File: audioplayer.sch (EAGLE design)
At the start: 16 parts, among them J1 MICRO-SDCARD-CONNECTOR-330006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, J2 JST-2P-SMD-PW-3410050P1, J3 MICRO-USB-5P-340015001, J4 CONNECTOR-HEADER-2X3P-3460180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, J5 AUDIO-CONNECTOR-6P-SMD-344003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, K1 BUTTON-4P-3100010P1, U1 ATMEGA328P-AU-1030060P1, U2 CN3065-1320040P1, U3 XC6206-3.3-1300260P1, U4 LM386M-1100070P1, X1 CRYSTAL-0500290P1

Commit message: 1 hr: Finished basic components and schematic.
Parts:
- removed U4: LM386M-1100070P1, OPL:LM386M-1100070P1
- added C10: 100nF, OPL:C-0603
- added C5: 22uF, OPL:C-POLAR-B
- added C6, C7: 10uF, OPL:C-POLAR-A
- added C8, C9: 1uF, OPL:C-0805
- added J6: SCREW-TERMINAL-2P-3470070P1, OPL:SCREW-TERMINAL-2P-3470070P1
- added J7: CONNECTOR-HEADER-6P-3460650P1, OPL:CONNECTOR-HEADER-6P-3460650P1
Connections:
- new net DTR: C10.1, J7.6
- new net N$1: C6.2, C7.1
- new net N$3: J7.2
- new net RX: J7.4, U1.PD0(RXD)
- new net TX: J7.5, U1.PD1(TXD)
- new net VBAT: C6.1, C8.2, J2.+, U2.BAT, U2.FB, U3.VIN
- net 3V3: now also C9.2, J7.3, U3.VOUT
- net 5V: now also C5.1, U2.VIN
- net AUDIO: now also J6.2
- net GND: now also C5.2, C7.2, C8.1, C9.1, J2.-, J6.1, J7.1, U2.GND, U2.TEMP, U3.VSS
- net RESET: now also C10.2
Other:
- moved on the sheet: J2, J3, U2, U3

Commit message: 0.25 hrs: initial placement of components on board.
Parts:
- added R1: (no value), OPL:R-0603
- renumbered R30 to R2
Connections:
- new net N$2: R1.2, U2.ISET
- net GND: now also R1.1
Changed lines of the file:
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@@
 <part name="J2" library="OPL" deviceset="JST-2P-SMD-PW" device="-3410050P1"/>
 <part name="U2" library="OPL" deviceset="CN3065" device="-1320040P1"/>
-<part name="R30" library="OPL" deviceset="R*" device="-0603" value="10K"/>
+<part name="R2" library="OPL" deviceset="R*" device="-0603" value="10K"/>
 <part name="U3" library="OPL" deviceset="XC6206-3.3" device="-1300260P1"/>
 <part name="J3" library="OPL" deviceset="MICRO-USB-5P" device="-340015001"/>
@@
 <part name="J7" library="OPL" deviceset="CONNECTOR-HEADER-6P" device="-3460650P1"/>
 <part name="C10" library="OPL" deviceset="C*" device="-0603" value="100nF"/>
+<part name="R1" library="OPL" deviceset="R*" device="-0603"/>
 </parts>
 <sheets>
@@
 <instance part="J2" gate="J" x="74.93" y="128.27" rot="R270"/>
 <instance part="U2" gate="U" x="35.56" y="118.11"/>
-<instance part="R30" gate="R" x="-19.05" y="83.82"/>
+<instance part="R2" gate="R" x="-19.05" y="83.82"/>
 <instance part="U3" gate="U" x="102.87" y="121.92"/>
 <instance part="J3" gate="USB" x="-19.05" y="118.11"/>
@@
 <instance part="J7" gate="J" x="138.43" y="118.11"/>
 <instance part="C10" gate="C" x="158.75" y="111.76"/>
+<instance part="R1" gate="R" x="20.32" y="119.38"/>
 </instances>
 <busses>
@@
 <junction x="-22.86" y="48.26"/>
 <label x="-25.4" y="96.52" size="1.778" layer="95"/>
-<pinref part="R30" gate="R" pin="1"/>
+<pinref part="R2" gate="R" pin="1"/>
 <junction x="-22.86" y="83.82"/>
 <pinref part="C1" gate="C" pin="2"/>
@@
 <segment>
 <pinref part="U2" gate="U" pin="TEMP"/>
-<wire x1="24.13" y1="121.92" x2="16.51" y2="121.92" width="0.1524" layer="91"/>
+<wire x1="24.13" y1="121.92" x2="15.24" y2="121.92" width="0.1524" layer="91"/>
 <label x="16.51" y="121.92" size="1.778" layer="95"/>
+<pinref part="R1" gate="R" pin="1"/>
+<wire x1="16.51" y1="119.38" x2="15.24" y2="119.38" width="0.1524" layer="91"/>
+<wire x1="15.24" y1="119.38" x2="15.24" y2="121.92" width="0.1524" layer="91"/>
 </segment>
 <segment>
@@
 </segment>
 <segment>
-<pinref part="R30" gate="R" pin="2"/>
+<pinref part="R2" gate="R" pin="2"/>
 <pinref part="U1" gate="U" pin="PC6(/RESET)"/>
 <wire x1="-15.24" y1="83.82" x2="3.81" y2="83.82" width="0.1524" layer="91"/>
@@
 </segment>
 </net>
+<net name="N$2" class="0">
+<segment>
+<pinref part="U2" gate="U" pin="ISET"/>
+<pinref part="R1" gate="R" pin="2"/>
+</segment>
+</net>

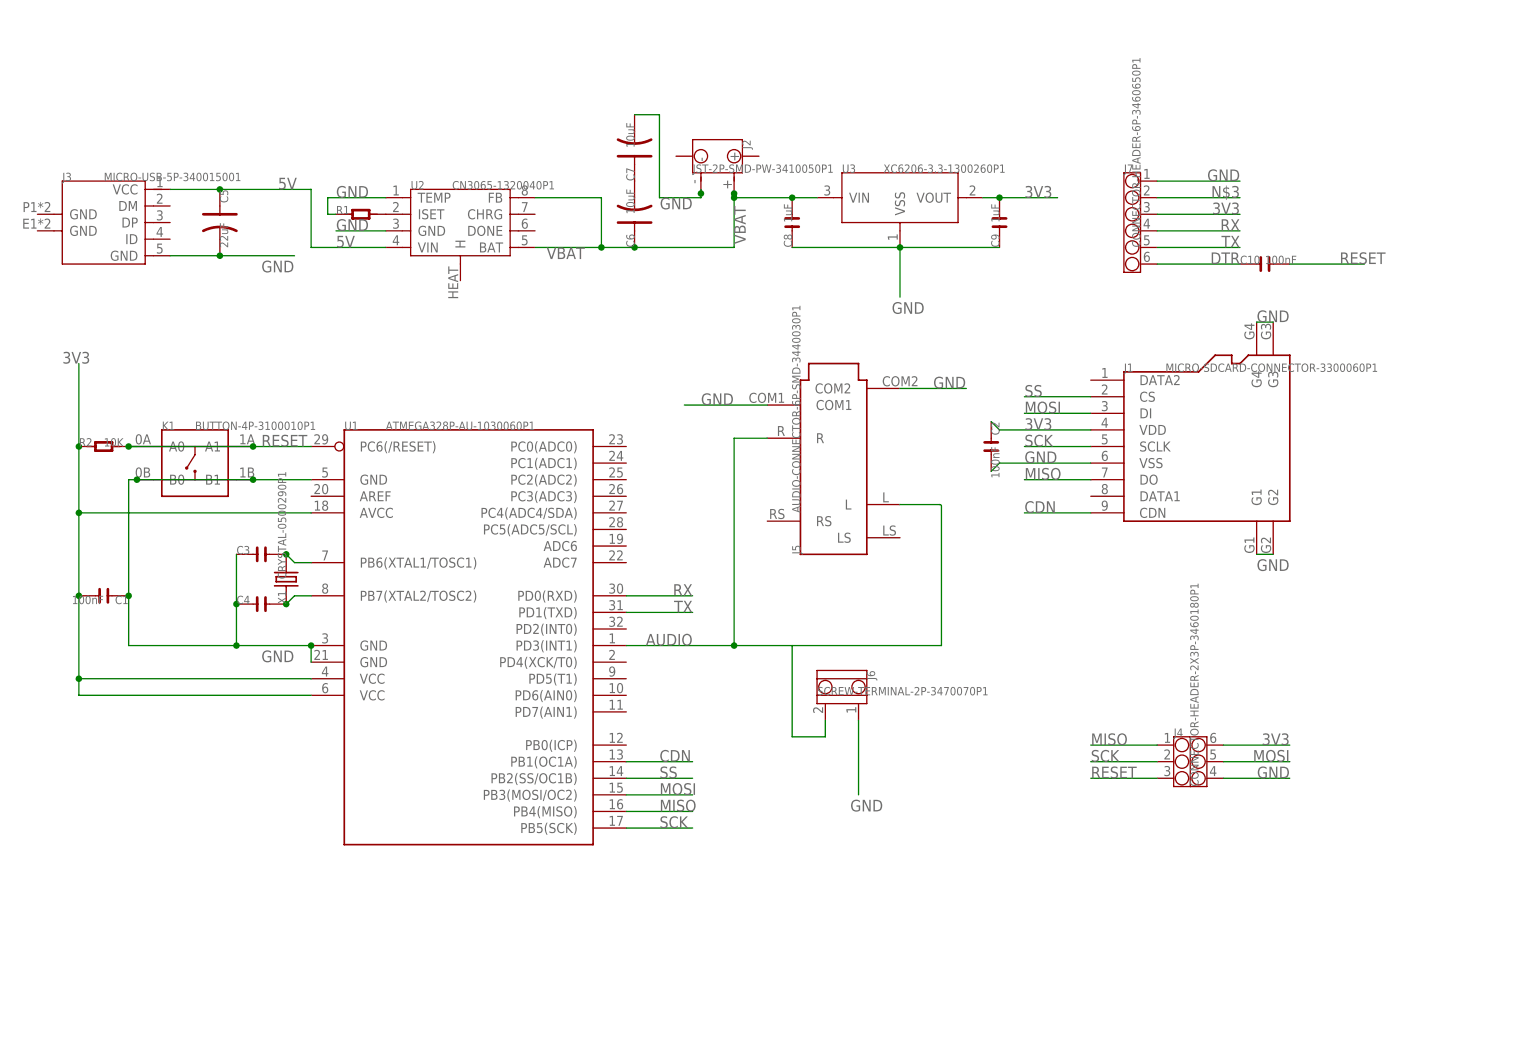
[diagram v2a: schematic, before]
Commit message: 1 hr. Add Arduino-compatible headers and redo layout (and commit brd file!).
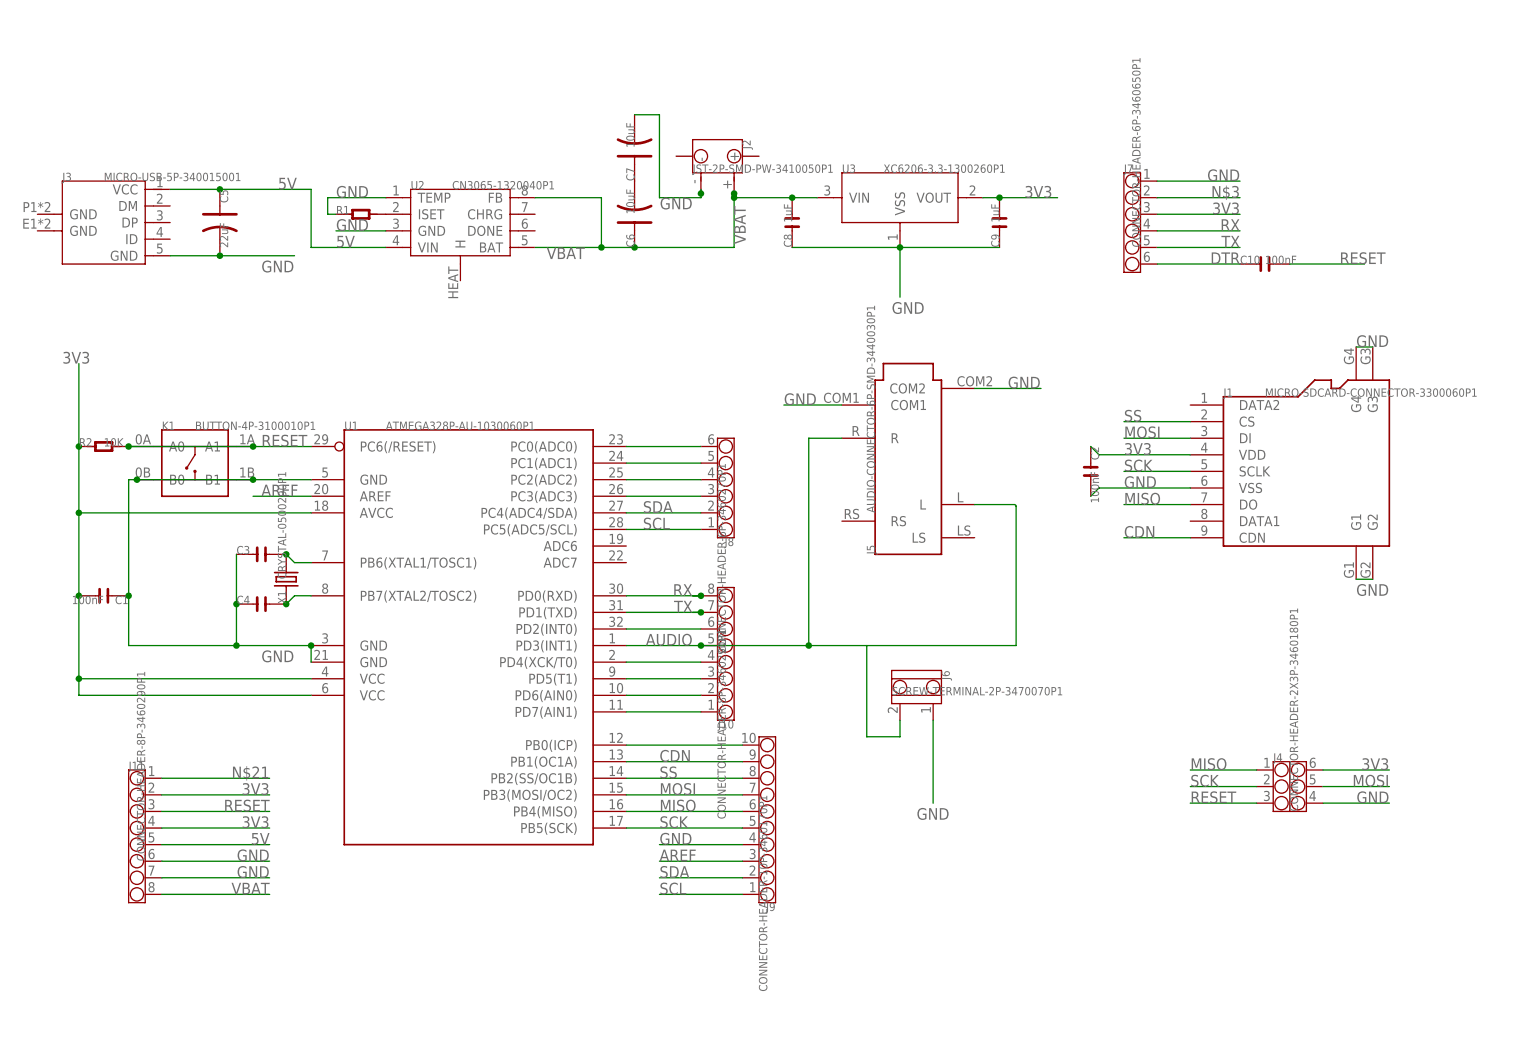
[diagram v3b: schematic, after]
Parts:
- added J10, J11: CONNECTOR-HEADER-8P-3460290P1, OPL:CONNECTOR-HEADER-8P-3460290P1
- added J8: CONNECTOR-HEADER-6P-3460270P1, OPL:CONNECTOR-HEADER-6P-3460270P1
- added J9: CONNECTOR-HEADER-10P-3460170P1, OPL:CONNECTOR-HEADER-10P-3460170P1
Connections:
- new net AREF: J9.3, U1.AREF
- new net N$10: J9.10, U1.PB0(ICP)
- new net N$11: J10.1, U1.PD7(AIN1)
- new net N$12: J10.2, U1.PD6(AIN0)
- new net N$13: J10.3, U1.PD5(T1)
- new net N$14: J10.4, U1.PD4(XCK/T0)
- new net N$15: J10.6, U1.PD2(INT0)
- new net N$21: J11.1
- new net N$6: J8.3, U1.PC3(ADC3)
- new net N$7: J8.4, U1.PC2(ADC2)
- new net N$8: J8.5, U1.PC1(ADC1)
- new net N$9: J8.6, U1.PC0(ADC0)
- new net SCL: J8.1, J9.1, U1.PC5(ADC5/SCL)
- new net SDA: J8.2, J9.2, U1.PC4(ADC4/SDA)
- net 3V3: now also J11.2, J11.4
- net 5V: now also J11.5
- net AUDIO: now also J10.5
- net CDN: now also J9.9
- net GND: now also J11.6, J11.7, J9.4
- net MISO: now also J9.6
- net MOSI: now also J9.7
- net RESET: now also J11.3
- net RX: now also J10.8
- net SCK: now also J9.5
- net SS: now also J9.8
- net TX: now also J10.7
- net VBAT: now also J11.8
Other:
- moved on the sheet: C2, J1, J4, J5, J6

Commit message: 1.5 hrs: routing.
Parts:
- C3, C4: value (none) -> 22pF
- R1: value (none) -> 4.7K
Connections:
- new net VFTDI: J7.3
- net 3V3: no longer J7.3
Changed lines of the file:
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@@
 <setting verticaltext="up"/>
 </settings>
-<grid distance="0.05" unitdist="inch" unit="inch" style="lines" multiple="1" display="no" altdistance="0.01" altunitdist="inch" altunit="inch"/>
+<grid distance="0.1" unitdist="inch" unit="inch" style="lines" multiple="1" display="no" altdistance="0.01" altunitdist="inch" altunit="inch"/>
 <layers>
 <layer number="1" name="Top" color="4" fill="1" visible="no" active="no"/>
@@
 <class number="0" name="default" width="0" drill="0">
 </class>
+<class number="1" name="power" width="0.254" drill="0">
+</class>
 </classes>
 <parts>
@@
 <part name="K1" library="OPL" deviceset="BUTTON-4P" device="-3100010P1"/>
 <part name="X1" library="OPL" deviceset="CRYSTAL*" device="-0500290P1"/>
-<part name="C3" library="OPL" deviceset="C*" device="-0603"/>
-<part name="C4" library="OPL" deviceset="C*" device="-0603"/>
+<part name="C3" library="OPL" deviceset="C*" device="-0603" value="22pF"/>
+<part name="C4" library="OPL" deviceset="C*" device="-0603" value="22pF"/>
 <part name="J5" library="OPL" deviceset="AUDIO-CONNECTOR-6P-SMD" device="-3440030P1"/>
 <part name="C5" library="OPL" deviceset="C-POLAR*" device="-B" value="22uF"/>
@@
 <part name="J7" library="OPL" deviceset="CONNECTOR-HEADER-6P" device="-3460650P1"/>
 <part name="C10" library="OPL" deviceset="C*" device="-0603" value="100nF"/>
-<part name="R1" library="OPL" deviceset="R*" device="-0603"/>
+<part name="R1" library="OPL" deviceset="R*" device="-0603" value="4.7K"/>
 <part name="J8" library="OPL" deviceset="CONNECTOR-HEADER-6P" device="-3460270P1"/>
 <part name="J10" library="OPL" deviceset="CONNECTOR-HEADER-8P" device="-3460290P1"/>
@@
 </busses>
 <nets>
-<net name="3V3" class="0">
+<net name="3V3" class="1">
 <segment>
 <pinref part="U1" gate="U" pin="AVCC"/>
@@
 </segment>
 <segment>
-<pinref part="J7" gate="J" pin="3"/>
-<wire x1="142.24" y1="119.38" x2="154.94" y2="119.38" width="0.1524" layer="91"/>
-<label x="154.94" y="119.38" size="1.778" layer="95" rot="MR0"/>
-</segment>
-<segment>
 <pinref part="J11" gate="J" pin="2"/>
 <wire x1="-10.16" y1="30.48" x2="6.35" y2="30.48" width="0.1524" layer="91"/>
@@
 </segment>
 </net>
-<net name="GND" class="0">
+<net name="GND" class="1">
 <segment>
 <pinref part="U1" gate="U" pin="GND@1"/>
@@
 </segment>
 </net>
-<net name="5V" class="0">
+<net name="5V" class="1">
 <segment>
 <pinref part="J3" gate="USB" pin="VCC"/>
@@
 </segment>
 </net>
-<net name="VBAT" class="0">
+<net name="VBAT" class="1">
 <segment>
 <pinref part="U2" gate="U" pin="BAT"/>
@@
 </segment>
 </net>
+<net name="VFTDI" class="1">
+<segment>
+<pinref part="J7" gate="J" pin="3"/>
+<wire x1="142.24" y1="119.38" x2="154.94" y2="119.38" width="0.1524" layer="91"/>
+<label x="154.94" y="119.38" size="1.778" layer="95" rot="MR0"/>
+</segment>
+</net>

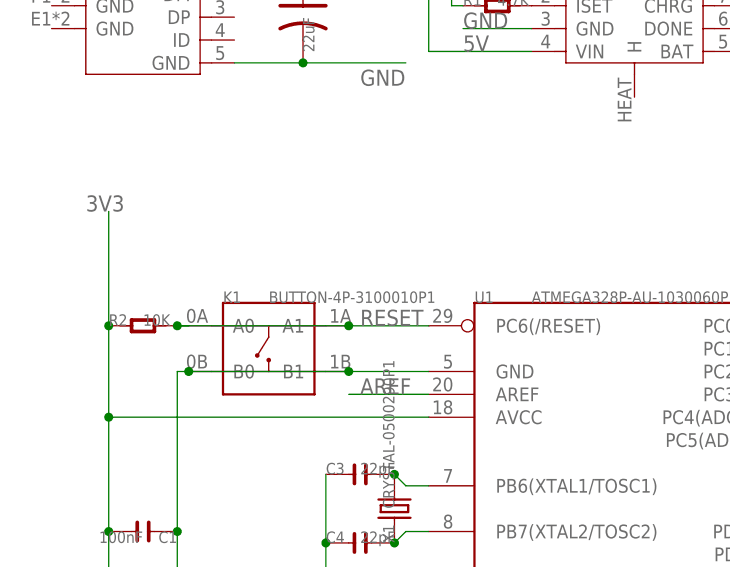
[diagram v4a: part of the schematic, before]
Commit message: 2 hrs. Routing the rest of the traces. Fix reset button.
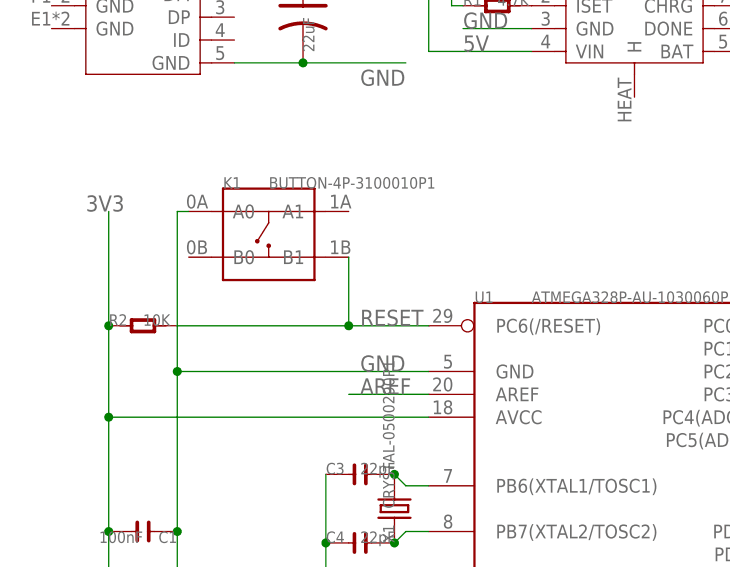
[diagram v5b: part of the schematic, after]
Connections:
- net GND: now also K1.A0; no longer K1.B0, K1.B1
- net RESET: now also K1.B1; no longer K1.A0, K1.A1
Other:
- moved on the sheet: K1
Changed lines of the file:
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@@
 <setting verticaltext="up"/>
 </settings>
-<grid distance="0.1" unitdist="inch" unit="inch" style="lines" multiple="1" display="no" altdistance="0.01" altunitdist="inch" altunit="inch"/>
+<grid distance="0.05" unitdist="inch" unit="inch" style="lines" multiple="1" display="no" altdistance="0.01" altunitdist="inch" altunit="inch"/>
 <layers>
 <layer number="1" name="Top" color="4" fill="1" visible="no" active="no"/>
@@
 <instance part="C1" gate="C" x="-19.05" y="60.96" rot="R180"/>
 <instance part="C2" gate="C" x="132.08" y="80.01" rot="R270"/>
-<instance part="K1" gate="K" x="-5.08" y="81.28"/>
+<instance part="K1" gate="K" x="-5.08" y="93.98"/>
 <instance part="X1" gate="X" x="8.89" y="63.5" rot="R90"/>
 <instance part="C3" gate="C" x="5.08" y="67.31"/>
@@
 <pinref part="U1" gate="U" pin="GND@2"/>
 <wire x1="12.7" y1="53.34" x2="12.7" y2="50.8" width="0.1524" layer="91"/>
-<pinref part="U1" gate="U" pin="GND"/>
-<wire x1="12.7" y1="78.74" x2="3.81" y2="78.74" width="0.1524" layer="91"/>
-<wire x1="3.81" y1="78.74" x2="-13.97" y2="78.74" width="0.1524" layer="91"/>
-<wire x1="-13.97" y1="78.74" x2="-15.24" y2="78.74" width="0.1524" layer="91"/>
 <wire x1="-15.24" y1="78.74" x2="-15.24" y2="60.96" width="0.1524" layer="91"/>
 <wire x1="-15.24" y1="60.96" x2="-15.24" y2="53.34" width="0.1524" layer="91"/>
@@
 <pinref part="C1" gate="C" pin="1"/>
 <junction x="-15.24" y="60.96"/>
-<pinref part="K1" gate="K" pin="B0"/>
-<junction x="-13.97" y="78.74"/>
-<pinref part="K1" gate="K" pin="B1"/>
-<junction x="3.81" y="78.74"/>
 <pinref part="C3" gate="C" pin="1"/>
 <pinref part="C4" gate="C" pin="1"/>
@@
 <junction x="1.27" y="59.69"/>
 <junction x="1.27" y="53.34"/>
+<pinref part="U1" gate="U" pin="GND"/>
+<wire x1="12.7" y1="78.74" x2="-15.24" y2="78.74" width="0.1524" layer="91"/>
+<label x="5.08" y="78.74" size="1.778" layer="95"/>
+<pinref part="K1" gate="K" pin="A0"/>
+<wire x1="-13.97" y1="96.52" x2="-15.24" y2="96.52" width="0.1524" layer="91"/>
+<wire x1="-15.24" y1="96.52" x2="-15.24" y2="78.74" width="0.1524" layer="91"/>
+<junction x="-15.24" y="78.74"/>
 </segment>
 <segment>
@@
 </segment>
 <segment>
+<pinref part="C10" gate="C" pin="2"/>
+<wire x1="162.56" y1="111.76" x2="173.99" y2="111.76" width="0.1524" layer="91"/>
+<label x="170.18" y="111.76" size="1.778" layer="95"/>
+</segment>
+<segment>
+<pinref part="J11" gate="J" pin="3"/>
+<wire x1="-10.16" y1="27.94" x2="6.35" y2="27.94" width="0.1524" layer="91"/>
+<label x="6.35" y="27.94" size="1.778" layer="95" rot="MR0"/>
+</segment>
+<segment>
 <pinref part="R2" gate="R" pin="2"/>
 <pinref part="U1" gate="U" pin="PC6(/RESET)"/>
 <wire x1="-15.24" y1="83.82" x2="3.81" y2="83.82" width="0.1524" layer="91"/>
 <label x="5.08" y="83.82" size="1.778" layer="95"/>
-<pinref part="K1" gate="K" pin="A0"/>
-<junction x="-15.24" y="83.82"/>
-<pinref part="K1" gate="K" pin="A1"/>
+<pinref part="K1" gate="K" pin="B1"/>
 <wire x1="3.81" y1="83.82" x2="12.7" y2="83.82" width="0.1524" layer="91"/>
+<wire x1="3.81" y1="91.44" x2="3.81" y2="83.82" width="0.1524" layer="91"/>
 <junction x="3.81" y="83.82"/>
-<wire x1="-15.24" y1="83.82" x2="-13.97" y2="83.82" width="0.1524" layer="91"/>
-</segment>
-<segment>
-<pinref part="C10" gate="C" pin="2"/>
-<wire x1="162.56" y1="111.76" x2="173.99" y2="111.76" width="0.1524" layer="91"/>
-<label x="170.18" y="111.76" size="1.778" layer="95"/>
-</segment>
-<segment>
-<pinref part="J11" gate="J" pin="3"/>
-<wire x1="-10.16" y1="27.94" x2="6.35" y2="27.94" width="0.1524" layer="91"/>
-<label x="6.35" y="27.94" size="1.778" layer="95" rot="MR0"/>
-</segment>
-</net>
+</segment>
+</net>
